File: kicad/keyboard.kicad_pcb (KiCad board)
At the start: 2 copper layers, 141 x 130.1 mm, 70 parts

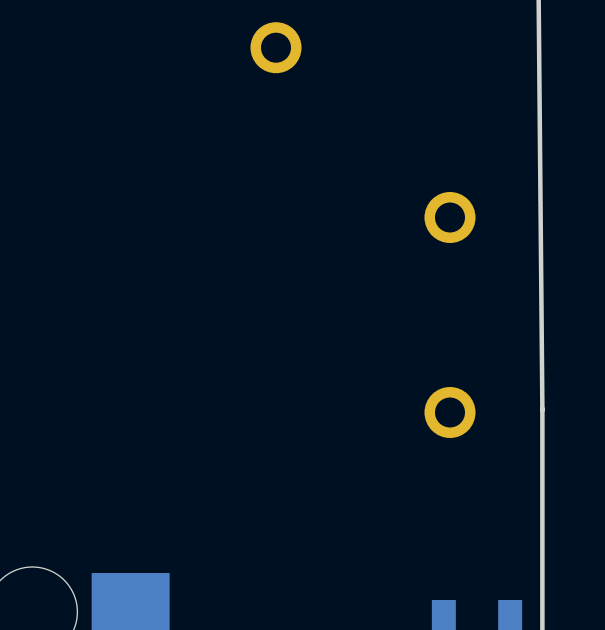
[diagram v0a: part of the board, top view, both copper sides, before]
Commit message: Use Typeractive reset button (Panasonic EVQ-PUC02K, SMD side)
- Switch reset from reset_switch_tht_top to ceoloide/reset_switch_smd_side,
  which matches the Typeractive reset button (Panasonic EVQ-PUC02K). The
  power switch was already the matching part (Alps SSSS811101 =
  power_switch_smd_side), so it is unchanged.
- Vendor reset_switch_smd_side.js footprint
- Wiring verified: RST1 -> {GND, RST}; PWR1 -> {BAT_P, RAW}; matrix intact
- Schematic: map the new footprint, lay Power/Reset parts side-by-side so
  pin labels don't collide (fixes a schematic-only net short); netlist clean
- Regenerate output/ and KiCad project
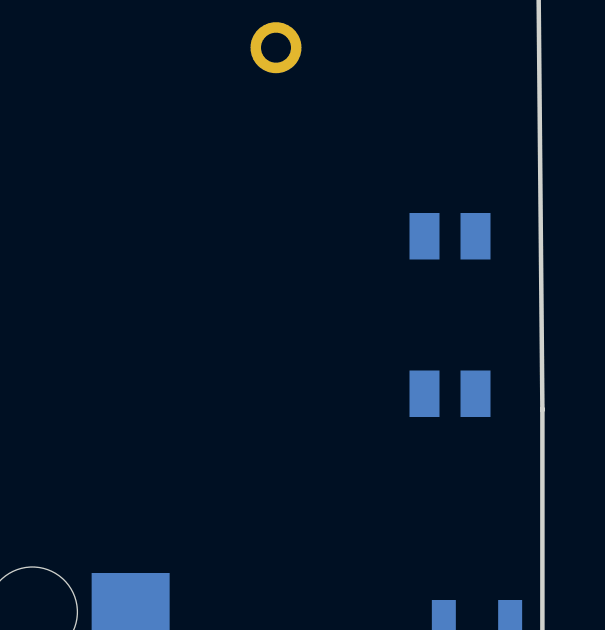
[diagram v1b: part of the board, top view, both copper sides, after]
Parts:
- RST1: footprint ceoloide:reset_switch_tht_top -> ceoloide:reset_switch_smd_side
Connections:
- RST1 pad 1: RST -> GND
- RST1 pad 2: GND -> RST
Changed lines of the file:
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@@
   (title_block
     (title "main")
-    (date "2026-08-16")
+    (date "2026-08-23")
     (rev "v1.0.0")
     (company "Unknown")
@@
     (pad "" np_thru_hole circle (at 0.025 1.5 90) (size 0.9 0.9) (drill 0.9) (layers "*.Cu" "*.Mask"))
   )
-  (footprint "ceoloide:reset_switch_tht_top"
+  (footprint "ceoloide:reset_switch_smd_side"
     (layer "B.Cu")
     (at 152.92000000000002 63.85 90)
     (property "Reference" "RST1"
-      (at 0 2.55 180)
-      (layer "B.SilkS")
-      hide
-      (effects (font (size 1 1) (thickness 0.15)))
-    )
-    (fp_text user "RST" (at 0 0 90) (layer "B.SilkS") (effects (font (size 1 1) (thickness 0.15)) (justify mirror)))
-    (fp_line (start 3 1.5) (end 3 1.75) (layer "B.SilkS") (stroke (width 0.15) (type solid)))
-    (fp_line (start 3 1.75) (end -3 1.75) (layer "B.SilkS") (stroke (width 0.15) (type solid)))
-    (fp_line (start -3 1.75) (end -3 1.5) (layer "B.SilkS") (stroke (width 0.15) (type solid)))
-    (fp_line (start -3 -1.5) (end -3 -1.75) (layer "B.SilkS") (stroke (width 0.15) (type solid)))
-    (fp_line (start -3 -1.75) (end 3 -1.75) (layer "B.SilkS") (stroke (width 0.15) (type solid)))
-    (fp_line (start 3 -1.75) (end 3 -1.5) (layer "B.SilkS") (stroke (width 0.15) (type solid)))
-    (pad "2" thru_hole circle (at -3.25 0 90) (size 1.7 1.7) (drill 1.0) (layers "*.Cu" "*.Mask") (net 3 "GND"))
-    (pad "1" thru_hole circle (at 3.25 0 90) (size 1.7 1.7) (drill 1.0) (layers "*.Cu" "*.Mask") (net 46 "RST"))
+      (at 0 0 90)
+      (layer "B.SilkS")
+      hide
+      (effects (font (size 1 1) (thickness 0.15)))
+    )
+    (attr smd)
+    (fp_line (start -2.35 -1.75) (end -2.35 1.75) (stroke (width 0.1) (type solid)) (layer "Dwgs.User"))
+    (fp_line (start -2.35 -1.75) (end 2.35 -1.75) (stroke (width 0.1) (type solid)) (layer "Dwgs.User"))
+    (fp_line (start -2.35 1.75) (end 2.35 1.75) (stroke (width 0.1) (type solid)) (layer "Dwgs.User"))
+    (fp_line (start -1.3 -2.75) (end -1.3 -1.75) (stroke (width 0.1) (type solid)) (layer "Dwgs.User"))
+    (fp_line (start -1.3 -2.75) (end 1.3 -2.75) (stroke (width 0.1) (type solid)) (layer "Dwgs.User"))
+    (fp_line (start 1.3 -2.75) (end 1.3 -1.75) (stroke (width 0.1) (type solid)) (layer "Dwgs.User"))
+    (fp_line (start 2.35 -1.75) (end 2.35 1.75) (stroke (width 0.1) (type solid)) (layer "Dwgs.User"))
+    (pad "1" smd rect (at -2.625 -0.85 270) (size 1.55 1) (layers "B.Cu" "B.Paste" "B.Mask") (net 3 "GND"))
+    (pad "2" smd rect (at -2.625 0.85 270) (size 1.55 1) (layers "B.Cu" "B.Paste" "B.Mask") (net 46 "RST"))
+    (pad "3" smd rect (at 2.625 -0.85 270) (size 1.55 1) (layers "B.Cu" "B.Paste" "B.Mask") (net 3 "GND"))
+    (pad "4" smd rect (at 2.625 0.85 270) (size 1.55 1) (layers "B.Cu" "B.Paste" "B.Mask") (net 46 "RST"))
+    (fp_line (start -2.35 -1.5) (end -2.35 -1.75) (stroke (width 0.1) (type solid)) (layer "B.SilkS"))
+    (fp_line (start -2.35 1.5) (end -2.35 1.75) (stroke (width 0.1) (type solid)) (layer "B.SilkS"))
+    (fp_line (start -2.1 -1.75) (end -2.35 -1.75) (stroke (width 0.1) (type solid)) (layer "B.SilkS"))
+    (fp_line (start -2.1 1.75) (end -2.35 1.75) (stroke (width 0.1) (type solid)) (layer "B.SilkS"))
+    (fp_line (start 2.1 -1.75) (end 2.35 -1.75) (stroke (width 0.1) (type solid)) (layer "B.SilkS"))
+    (fp_line (start 2.1 1.75) (end 2.35 1.75) (stroke (width 0.1) (type solid)) (layer "B.SilkS"))
+    (fp_line (start 2.35 -1.5) (end 2.35 -1.75) (stroke (width 0.1) (type solid)) (layer "B.SilkS"))
+    (fp_line (start 2.35 1.5) (end 2.35 1.75) (stroke (width 0.1) (type solid)) (layer "B.SilkS"))
   )
   (footprint "ceoloide:mounting_hole_plated"

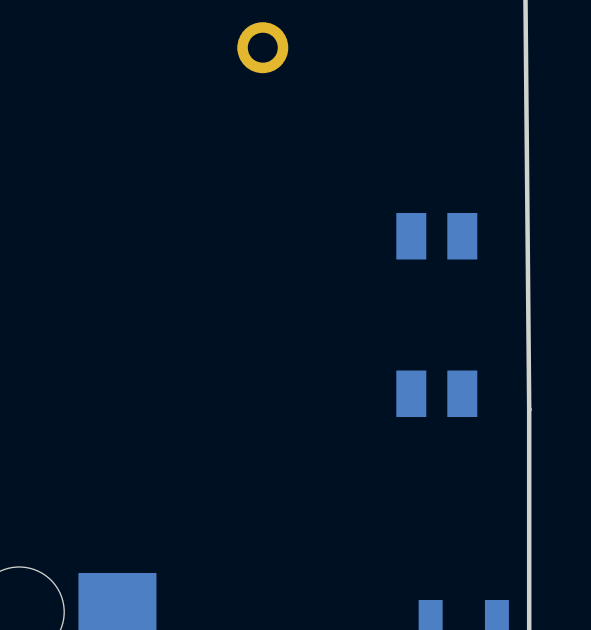
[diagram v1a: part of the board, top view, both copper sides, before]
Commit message: Add 3D models so the board visualizes in KiCad
- Vendor infused-kim STEP models into kicad/3d_models/ (~5.7MB): Choc V1
  switch/hotswap/keycap, 1N4148W diode, nice!nano V2, power + reset switches,
  2x12 pin socket.
- Wire each footprint's *_3dmodel_filename param in config.yaml using
  ${KIPRJMOD}/3d_models/... so paths resolve relative to the KiCad project.
- PCB now has 120 (model ...) entries (29 switches x3 + 30 diodes + nice!nano
  + power + reset). Verified: kicad-cli renders the board in 3D with keycaps,
  switches, sockets and diodes in place.
- Not yet modelled: JST-PH battery connector and EVQWGD001 encoder (no stock
  community model); minor.
Regenerate output/ + KiCad project.
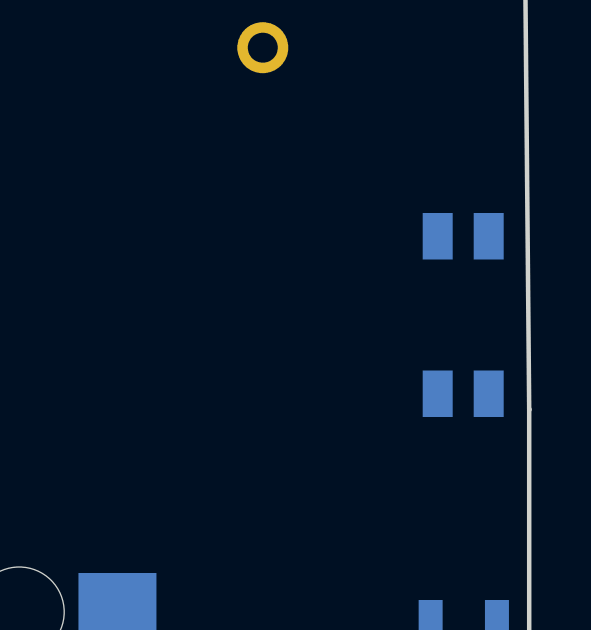
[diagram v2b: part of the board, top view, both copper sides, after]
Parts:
- moved RST1 0.88 mm to (153.8, 63.9), turned to -90 degrees

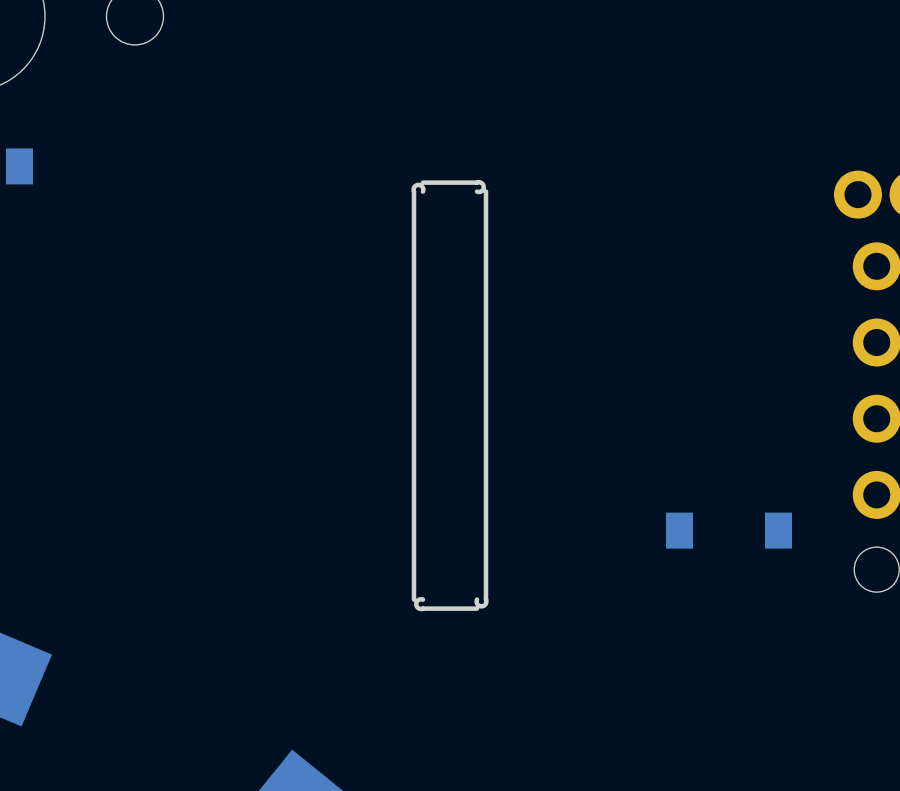
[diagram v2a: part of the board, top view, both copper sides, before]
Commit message: Fix 3D model alignment for back-side components
Ceoloide footprints emit STEP models with raw transforms and do not apply
KiCad's back-side flip compensation. Add explicit back-side rotation/offset
(matching infused-kim's gen_3d_model rotation_b/offset_b) for all components
mounted on the Back: choc switch/hotswap/keycap, diodes, nice!nano, and the
power/reset slide switches. Ignore KiCad ~*.lck lock files.
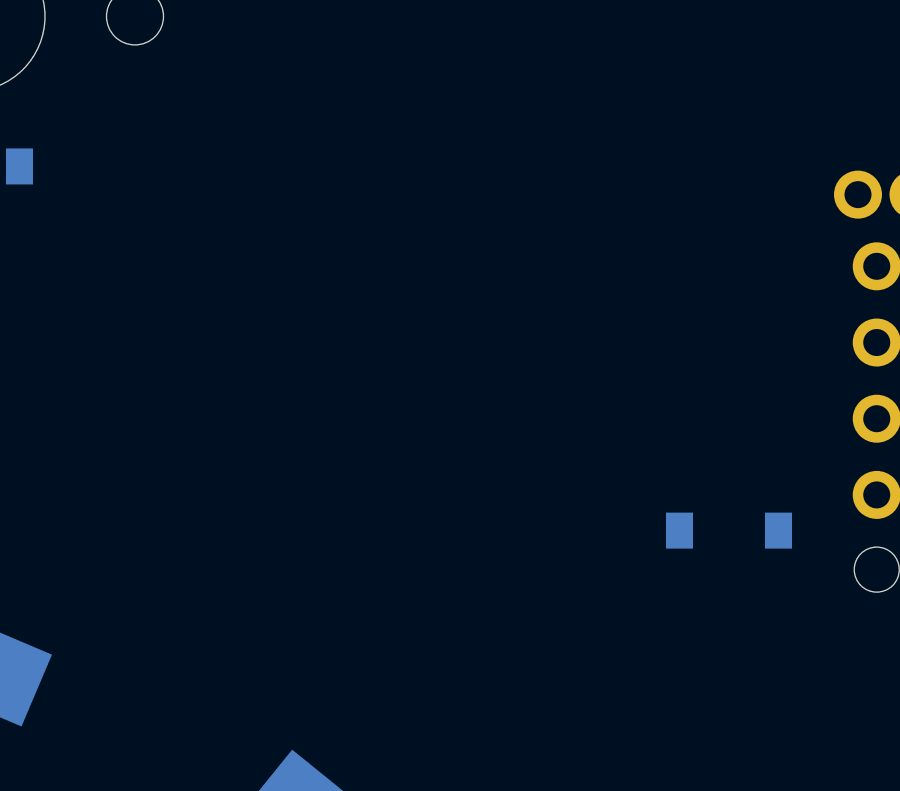
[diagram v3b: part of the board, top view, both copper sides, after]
